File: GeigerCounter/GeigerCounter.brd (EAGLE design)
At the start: 38.1 x 35.6 mm, 37 parts, among them IC1 OPAMP-DUALU

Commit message: Beginning to debug errors. Have not poured ground pour yet.
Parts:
- moved R5 11.8 mm to (27.6, 53.9)
- moved R4 11.8 mm to (30.3, 53.9)
- moved TP_RC 10.3 mm to (49.3, 48.6)
- moved TP_AMP 9.14 mm to (41.5, 50.4)
- moved TP_VCC1 7.65 mm to (50.6, 37.8)
- moved C6 3.27 mm to (35.9, 53.4), turned to 0 degrees
- moved TP_GND1 1.97 mm to (24.9, 40.1)
- moved TP_GND 1.57 mm to (21.7, 37.9)
- moved D1 1.30 mm to (18.1, 43.8)
- moved C7 1.19 mm to (35.9, 51.0), turned to 0 degrees
- moved TP_ENV 1.00 mm to (42.2, 43.1)
- moved D2 0.94 mm to (45.7, 49.0)
- moved R9 0.81 mm to (49.4, 45.8)
- moved R11 0.74 mm to (46.1, 45.8)
- moved TP_VCC 0.66 mm to (46.8, 37.8)
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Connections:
- net GND: no longer U$1.P$7, U$1.P$8
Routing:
- net VCC: track 5.56 -> 79.0 mm
- net VCC_1.25: track 12.8 -> 53.7 mm
- net OUTPUT: track 6.45 -> 23.4 mm
- net PRE_AMP: track 7.42 -> 12.8 mm
- net RC_OUT: track 5.48 -> 8.08 mm
- net IC1B_OUT: track 15.2 -> 17.4 mm
- net ENV_DETEC_OUT: track 9.15 -> 11.1 mm
- net P3.4: track 5.28 -> 4.17 mm
- net IC1A_N: track 20.0 -> 18.9 mm
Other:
- outline, holes or cut-outs redrawn

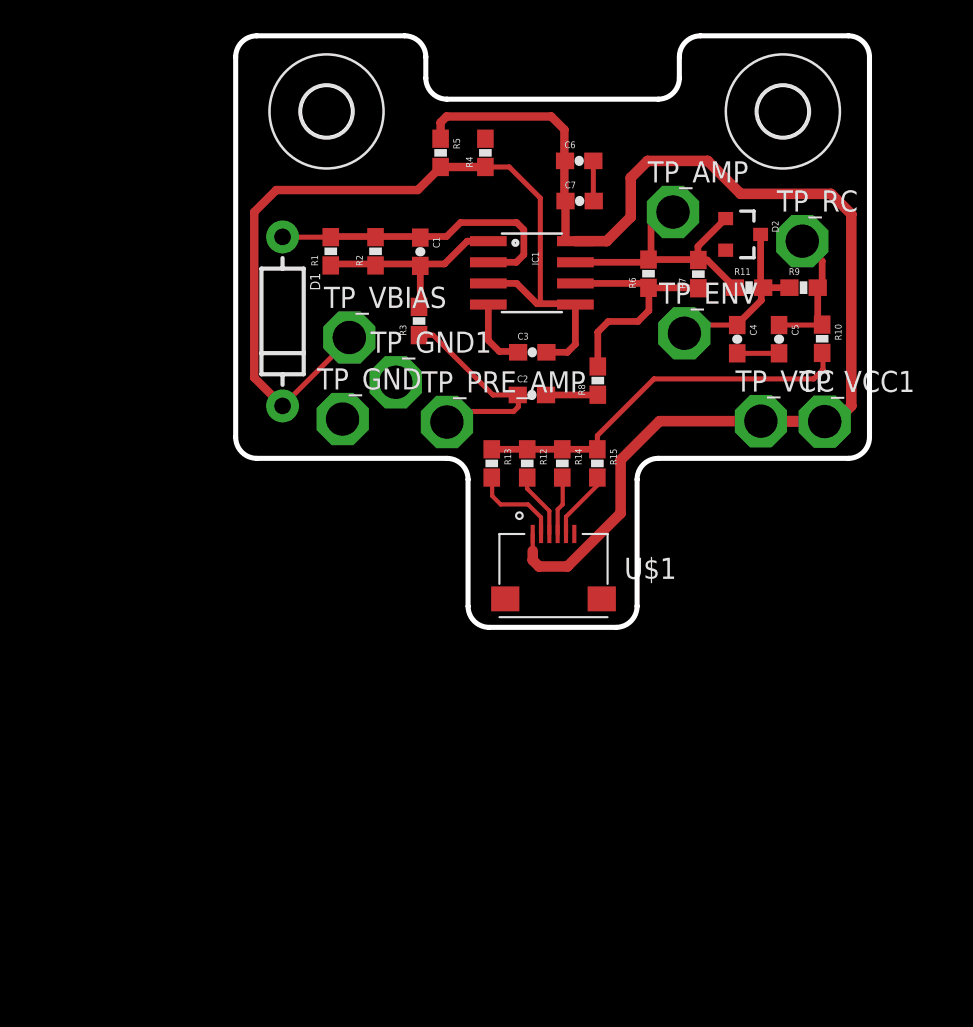
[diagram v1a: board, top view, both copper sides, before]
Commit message: All errors from DRC/ERC cleared... need to double check board now
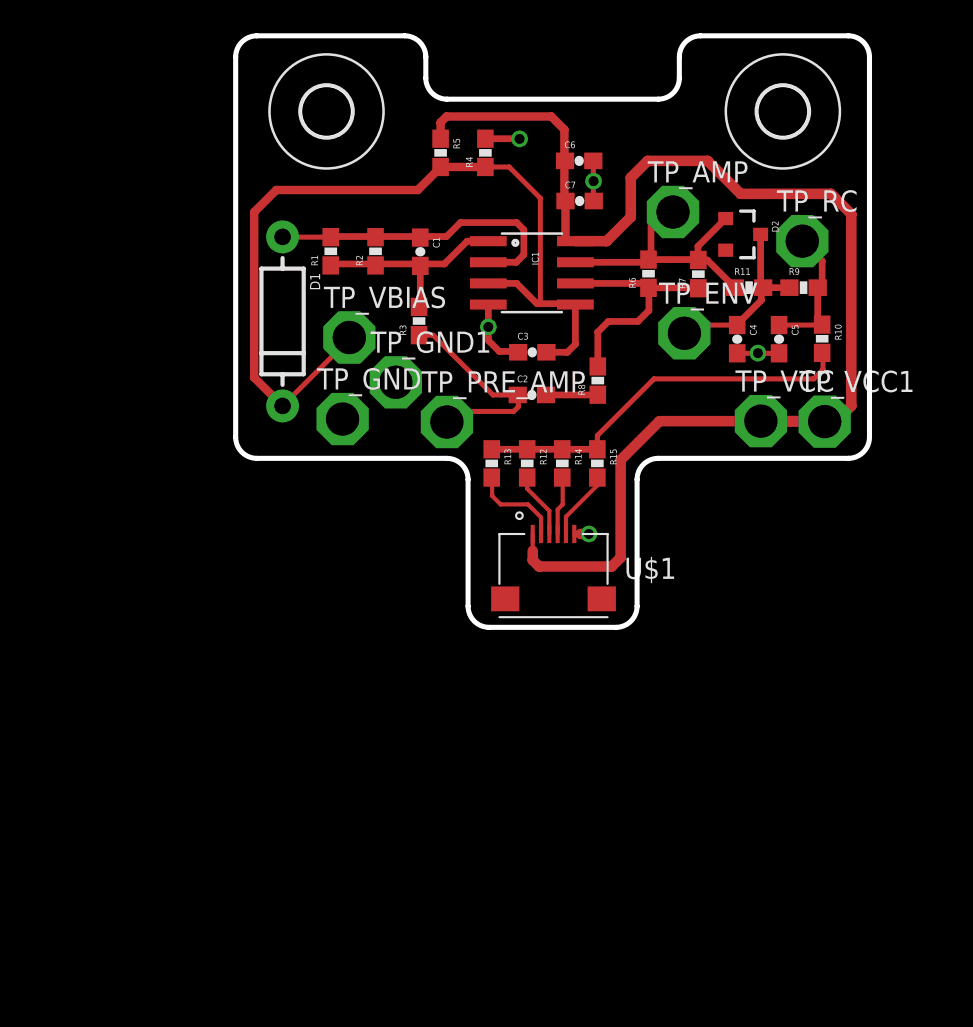
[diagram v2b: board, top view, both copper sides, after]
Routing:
- net GND: track 9.18 -> 12.2 mm, vias 0 -> 5
- net VCC: track 79.0 -> 80.6 mm
- added copper zone on layer 16, net GND

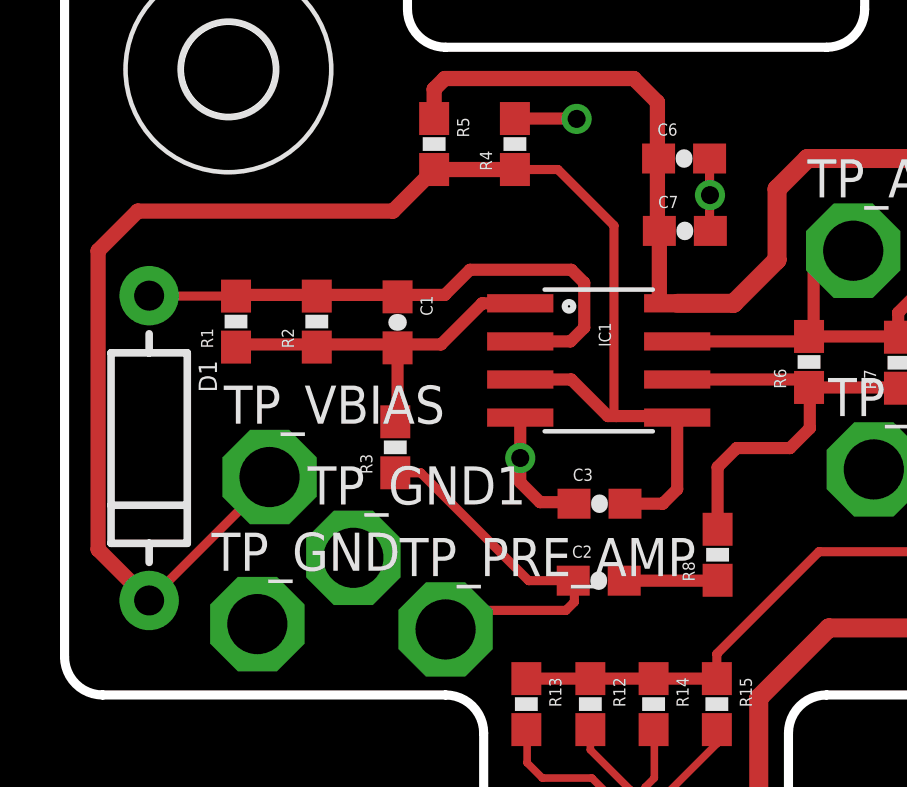
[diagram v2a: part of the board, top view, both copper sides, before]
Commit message: all errors cleared except Stop Mask errors that I think I will ignore
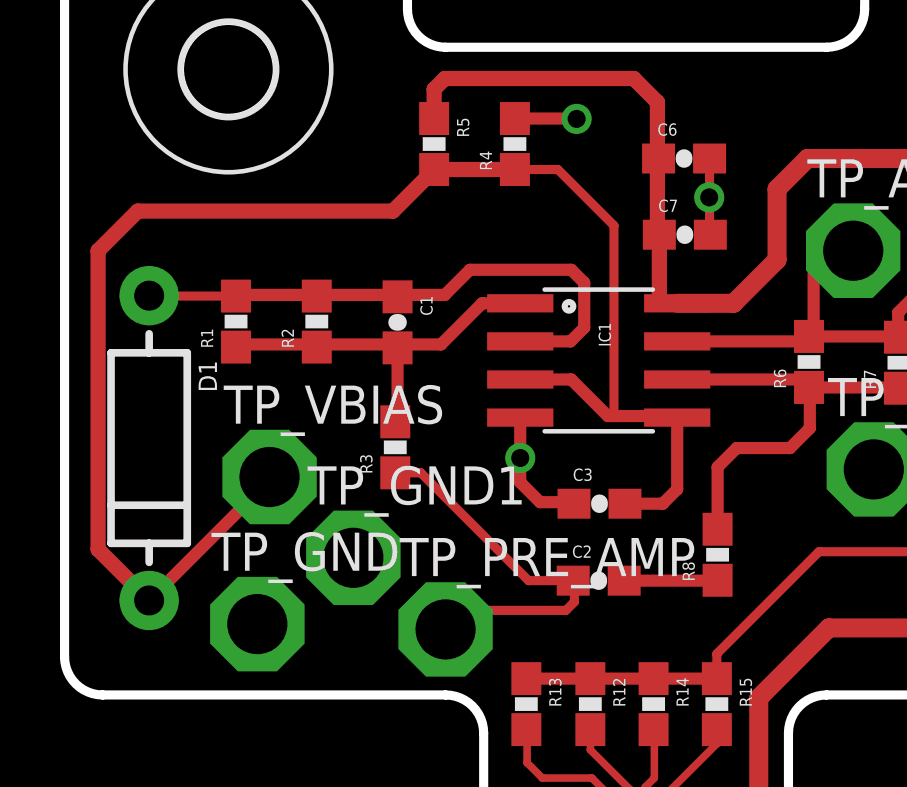
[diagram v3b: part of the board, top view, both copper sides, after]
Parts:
- moved C7 0.13 mm to (35.9, 50.9)
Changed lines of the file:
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@@
 <param name="mdSmdStop" value="0mil"/>
 <param name="msWidth" value="9mil"/>
-<param name="msDrill" value="24mil"/>
+<param name="msDrill" value="23mil"/>
 <param name="msMicroVia" value="9.99mm"/>
 <param name="msBlindViaRatio" value="0.5"/>
@@
 <param name="mvStopFrame" value="1"/>
 <param name="mvCreamFrame" value="0"/>
-<param name="mlMinStopFrame" value="4mil"/>
+<param name="mlMinStopFrame" value="0mil"/>
 <param name="mlMaxStopFrame" value="4mil"/>
 <param name="mlMinCreamFrame" value="0mil"/>
@@
 <element name="R10" library="SparkFun-Passives" package="0603-RES" value="0" x="50.4952" y="42.7482" rot="R270"/>
 <element name="C6" library="SparkFun-Passives" package="0603-CAP" value="2.2uF" x="35.8902" y="53.4416"/>
-<element name="C7" library="SparkFun-Passives" package="0603-CAP" value="0.1uF" x="35.9156" y="51.0286"/>
+<element name="C7" library="SparkFun-Passives" package="0603-CAP" value="0.1uF" x="35.9156" y="50.9016"/>
 <element name="R11" library="SparkFun-Passives" package="0603-RES" value="0" x="46.101" y="45.8216"/>
 <element name="TP_ENV" library="testpad" package="P1-20" value="PTR1PAD1-20" x="42.2148" y="43.0784">
@@
 <wire x1="34.2138" y1="56.1086" x2="35.0012" y2="55.3212" width="0.508" layer="1"/>
 <wire x1="35.0012" y1="55.3212" x2="35.0012" y2="51.093" width="0.508" layer="1"/>
-<wire x1="35.0012" y1="51.093" x2="35.0656" y2="51.0286" width="0.508" layer="1"/>
-<wire x1="35.0656" y1="51.0286" x2="35.0656" y2="48.7562" width="0.508" layer="1"/>
+<wire x1="35.0012" y1="51.093" x2="35.0656" y2="50.9016" width="0.508" layer="1"/>
+<wire x1="35.0656" y1="50.9016" x2="35.0656" y2="48.7562" width="0.508" layer="1"/>
 <wire x1="35.0656" y1="48.7562" x2="35.0402" y2="48.7308" width="0.508" layer="1"/>
 <wire x1="33.0962" y1="31.0134" x2="33.0962" y2="29.9974" width="0.254" layer="1"/>
@@
 <wire x1="45.3898" y1="41.8728" x2="47.9044" y2="41.8728" width="0.3048" layer="1"/>
 <wire x1="36.7402" y1="53.4416" x2="36.7402" y2="51.054" width="0.3048" layer="1"/>
-<wire x1="36.7402" y1="51.054" x2="36.7656" y2="51.0286" width="0.3048" layer="1"/>
+<wire x1="36.7402" y1="51.054" x2="36.7656" y2="50.9016" width="0.3048" layer="1"/>
 <wire x1="35.5962" y1="31.0134" x2="35.9664" y2="31.0134" width="0.254" layer="1"/>
 <wire x1="35.9664" y1="31.0134" x2="36.4744" y2="31.0134" width="0.635" layer="1"/>
@@
 </polygon>
 <via x="32.3088" y="54.7624" extent="1-16" drill="0.6"/>
-<via x="36.7538" y="52.2224" extent="1-16" drill="0.6"/>
+<via x="36.7284" y="52.1462" extent="1-16" drill="0.6"/>
 <via x="46.6344" y="41.8846" extent="1-16" drill="0.6"/>
-<wire x1="36.7538" y1="52.2224" x2="36.7402" y2="51.054" width="0" layer="19" extent="1-1"/>
+<wire x1="36.7284" y1="52.1462" x2="36.7402" y2="51.054" width="0" layer="19" extent="1-1"/>
 <wire x1="32.3478" y1="54.7742" x2="32.3088" y2="54.7624" width="0" layer="19" extent="1-1"/>
 <wire x1="45.3898" y1="41.8728" x2="46.6344" y2="41.8846" width="0" layer="19" extent="1-1"/>
@@
 <wire x1="33.5534" y1="44.9326" x2="33.6296" y2="44.8564" width="0.3048" layer="1"/>
 <wire x1="22.0726" y1="42.8244" x2="22.0726" y2="42.7228" width="0.3048" layer="1"/>
-<wire x1="22.0726" y1="42.7228" x2="18.0594" y2="38.7096" width="0.3048" layer="1"/>
 <wire x1="27.559" y1="53.0742" x2="27.559" y2="53.0606" width="0.508" layer="1"/>
 <wire x1="27.559" y1="53.0606" x2="26.1874" y2="51.689" width="0.508" layer="1"/>
@@
 <wire x1="16.3576" y1="40.4114" x2="18.0594" y2="38.7096" width="0.508" layer="1"/>
 <wire x1="27.559" y1="53.0742" x2="30.2514" y2="53.0742" width="0.508" layer="1"/>
+<wire x1="22.0726" y1="42.7228" x2="18.0594" y2="38.7096" width="0.4064" layer="1"/>
 </signal>
 <signal name="IC1A_N">

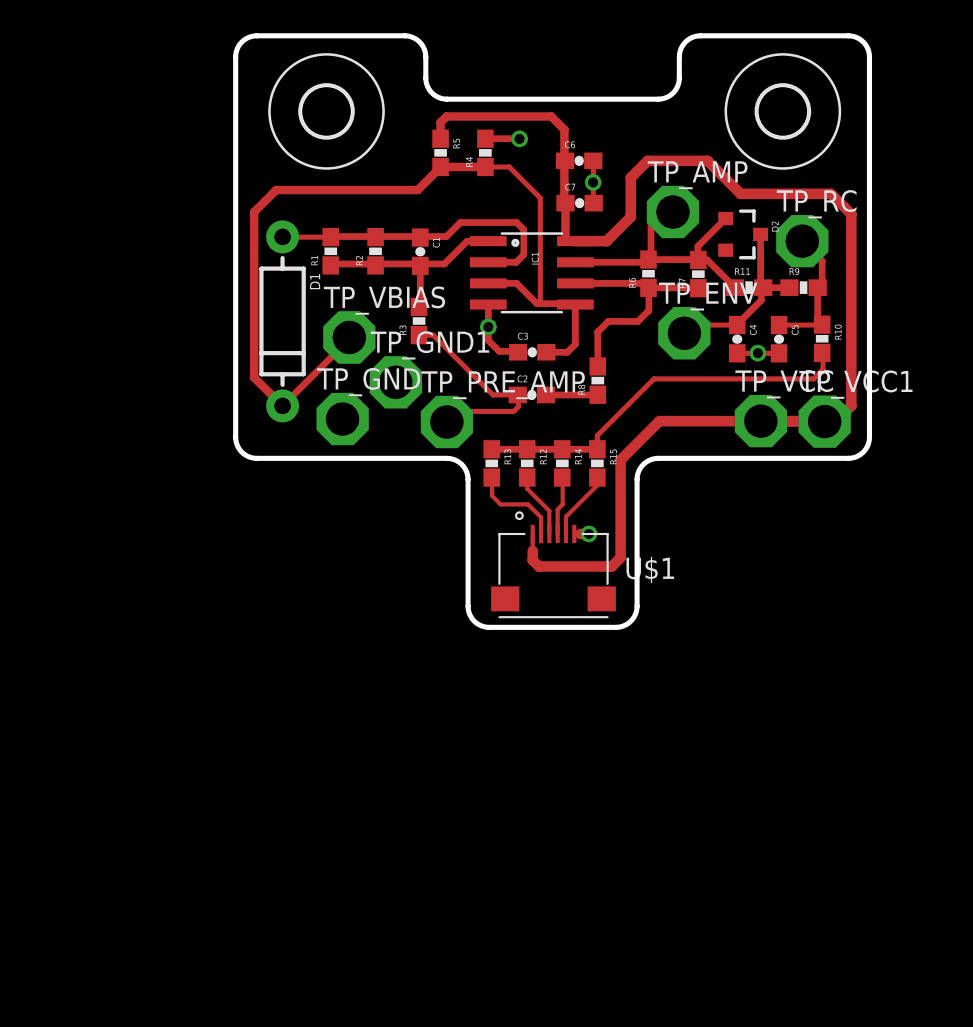
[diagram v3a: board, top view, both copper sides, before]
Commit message: Added silkscreen
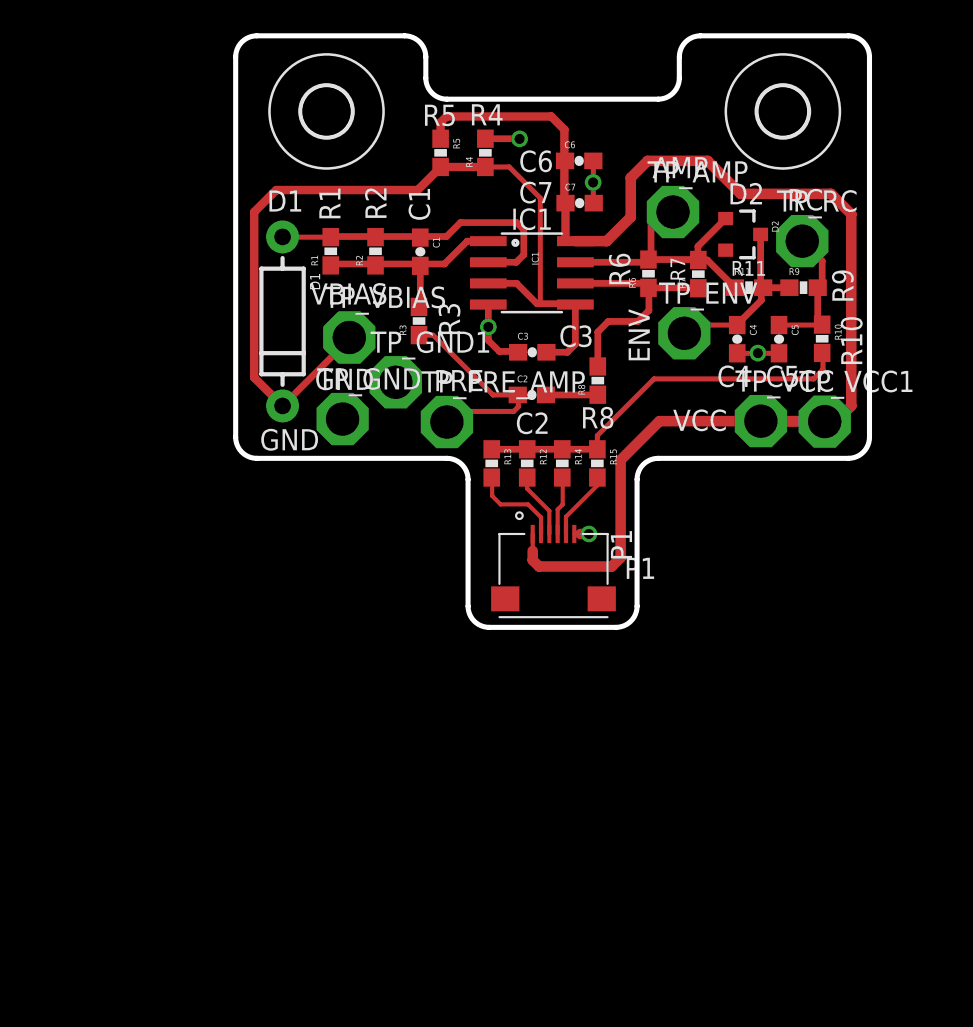
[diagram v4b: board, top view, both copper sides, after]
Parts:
- renumbered U$1 to P1
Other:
- board text added: "AMP"
- board text added: "C1"
- board text added: "C2"
- board text added: "C3"
- board text added: "C4"
- board text added: "C5"
- board text added: "C6"
- board text added: "C7"
- board text added: "D1"
- board text added: "D2"
- board text added: "ENV"
- board text added: "GND"
- board text added: "IC1"
- board text added: "P1"
- board text added: "PRE"
- board text added: "R1"
- board text added: "R10"
- board text added: "R11"
- board text added: "R2"
- board text added: "R3"
- board text added: "R4"
- board text added: "R5"
- board text added: "R6"
- board text added: "R7"
- board text added: "R8"
- board text added: "R9"
- board text added: "RC"
- board text added: "VBIAS"
- board text added: "VCC"
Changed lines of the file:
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@@
 <wire x1="39.37" y1="34.29" x2="40.64" y2="35.56" width="0.3048" layer="20" curve="-90"/>
 <wire x1="52.07" y1="35.56" x2="53.34" y2="36.83" width="0.3048" layer="20" curve="90"/>
+<text x="21.5392" y="49.8348" size="1.27" layer="21" rot="R90">R1</text>
+<text x="24.3078" y="49.8602" size="1.27" layer="21" rot="R90">R2</text>
+<text x="26.924" y="49.8094" size="1.27" layer="21" rot="R90">C1</text>
+<text x="26.4668" y="55.5498" size="1.27" layer="21">R5</text>
+<text x="29.2862" y="55.5752" size="1.27" layer="21">R4</text>
+<text x="28.7274" y="42.8752" size="1.27" layer="21" rot="R90">R3</text>
+<text x="34.671" y="42.2656" size="1.27" layer="21">C3</text>
+<text x="32.0548" y="37.0332" size="1.27" layer="21">C2</text>
+<text x="35.9664" y="37.3634" size="1.27" layer="21">R8</text>
+<text x="39.0652" y="29.3878" size="1.27" layer="21" rot="R90">P1</text>
+<text x="17.1196" y="50.3936" size="1.27" layer="21">D1</text>
+<text x="44.831" y="50.8254" size="1.27" layer="21">D2</text>
+<text x="32.258" y="52.7812" size="1.27" layer="21">C6</text>
+<text x="32.258" y="50.9016" size="1.27" layer="21">C7</text>
+<text x="31.7754" y="49.3014" size="1.27" layer="21">IC1</text>
+<text x="19.7104" y="44.8056" size="1.27" layer="21">VBIAS</text>
+<text x="19.9898" y="39.6748" size="1.27" layer="21">GND</text>
+<text x="16.6878" y="36.0426" size="1.27" layer="21">GND</text>
+<text x="27.1526" y="39.5986" size="1.27" layer="21">PRE</text>
+<text x="41.529" y="37.211" size="1.27" layer="21">VCC</text>
+<text x="40.132" y="41.3004" size="1.27" layer="21" rot="R90">ENV</text>
+<text x="48.387" y="50.4698" size="1.27" layer="21">RC</text>
+<text x="40.2844" y="52.4002" size="1.27" layer="21">AMP</text>
+<text x="38.9636" y="45.8724" size="1.27" layer="21" rot="R90">R6</text>
+<text x="52.9082" y="41.0718" size="1.27" layer="21" rot="R90">R10</text>
+<text x="52.3748" y="44.8818" size="1.27" layer="21" rot="R90">R9</text>
+<text x="47.0916" y="39.8526" size="1.27" layer="21">C5</text>
+<text x="44.1706" y="39.8526" size="1.27" layer="21">C4</text>
+<text x="45.0088" y="46.5328" size="0.889" layer="21">R11</text>
+<text x="42.2656" y="46.2026" size="0.889" layer="21" rot="R90">R7</text>
 </plain>
 <attributes>
@@
 <element name="IC1" library="SparkFun-AnalogIC" package="SO08" value="OPAMP-DUALU" x="33.0454" y="46.7106" rot="R270"/>
 <element name="D1" library="GeigerCounter" package="DIODE-1N4001" value="S1223" x="18.0594" y="43.7896" rot="R270"/>
-<element name="U$1" library="GeigerCounter" package="XF2M-0615-1A" value="XF2M-0615-1A" x="34.3662" y="28.4734"/>
+<element name="P1" library="GeigerCounter" package="XF2M-0615-1A" value="XF2M-0615-1A" x="34.3662" y="28.4734"/>
 <element name="H1" library="holes" package="3,0" value="MOUNT-HOLE3.0" x="20.701" y="56.4134"/>
 <element name="H2" library="holes" package="3,0" value="MOUNT-HOLE3.0" x="48.133" y="56.4134"/>
@@
 <signals>
 <signal name="VCC">
-<contactref element="U$1" pad="1"/>
+<contactref element="P1" pad="1"/>
 <contactref element="IC1" pad="8"/>
 <contactref element="TP_VCC" pad="TP"/>
@@
 </signal>
 <signal name="GND">
-<contactref element="U$1" pad="6"/>
+<contactref element="P1" pad="6"/>
 <contactref element="IC1" pad="4"/>
 <contactref element="TP_GND" pad="TP"/>
@@
 </signal>
 <signal name="P3.5">
-<contactref element="U$1" pad="3"/>
+<contactref element="P1" pad="3"/>
 <contactref element="R12" pad="2"/>
 <wire x1="32.766" y1="34.4052" x2="32.766" y2="33.7312" width="0.254" layer="1"/>
@@
 </signal>
 <signal name="P3.4">
-<contactref element="U$1" pad="5"/>
+<contactref element="P1" pad="5"/>
 <contactref element="R15" pad="2"/>
 <wire x1="35.0962" y1="31.0134" x2="35.0962" y2="32.0482" width="0.254" layer="1"/>
@@
 </signal>
 <signal name="NC1">
-<contactref element="U$1" pad="2"/>
+<contactref element="P1" pad="2"/>
 <contactref element="R13" pad="2"/>
 <wire x1="33.5962" y1="31.0134" x2="33.5962" y2="32.012" width="0.254" layer="1"/>
@@
 </signal>
 <signal name="NC2">
-<contactref element="U$1" pad="4"/>
+<contactref element="P1" pad="4"/>
 <contactref element="R14" pad="2"/>
 <wire x1="34.5962" y1="31.0134" x2="34.5962" y2="32.488" width="0.254" layer="1"/>
